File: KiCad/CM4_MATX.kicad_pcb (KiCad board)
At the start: 2 copper layers, 243.8 x 243.8 mm, 66 parts, among them IC1 USB2517-JZX, IC2 PI7C9X2G404SLBFDE, IC3 M24C04-RMN6TP, J1 72309-8014BLF, J10 72309-8014BLF, J11 10104110-0001LF, J12 SS-52100-002, J13 PCIe_x16, J14 PCIe_x16, J15 PCIe_x16, J16 GSD090012SEU, J17 Conn_02x04_Odd_Even, J18 ARJM11C7-502-AB-ER2-T, J19 Conn_02x20_Odd_Even, J20 Conn_02x04_Odd_Even, J3 Conn_01x22_Female, J5 Conn_01x22_Female, J6 1888811-1, J7 39-28-1243, J9 Conn_02x05_Odd_Even, M1 Fan_CPU_4pin, M2 Fan_CPU_4pin, U1 MAX6639ATE+, U10 MIC2019YM6-TR, U11 MIC2019YM6-TR, U12 MIC2019YM6-TR, U13 MIC2019YM6-TR, U14 MIC2019YM6-TR, U15 MIC2019YM6-TR, U16 MIC2019YM6-TR, U17 TCA9548ARGER, U18 PCF85263AT, U19 AP7363-10D, U3 FSUSB42MUX, U4 AP7363-10D, U5 AP2822CKETR-G1, U6 74LVC1G07GW, U7 TPD4EUSB30, U8 RT9742GGJ5, U9 TPD4EUSB30, Y2 Crystal

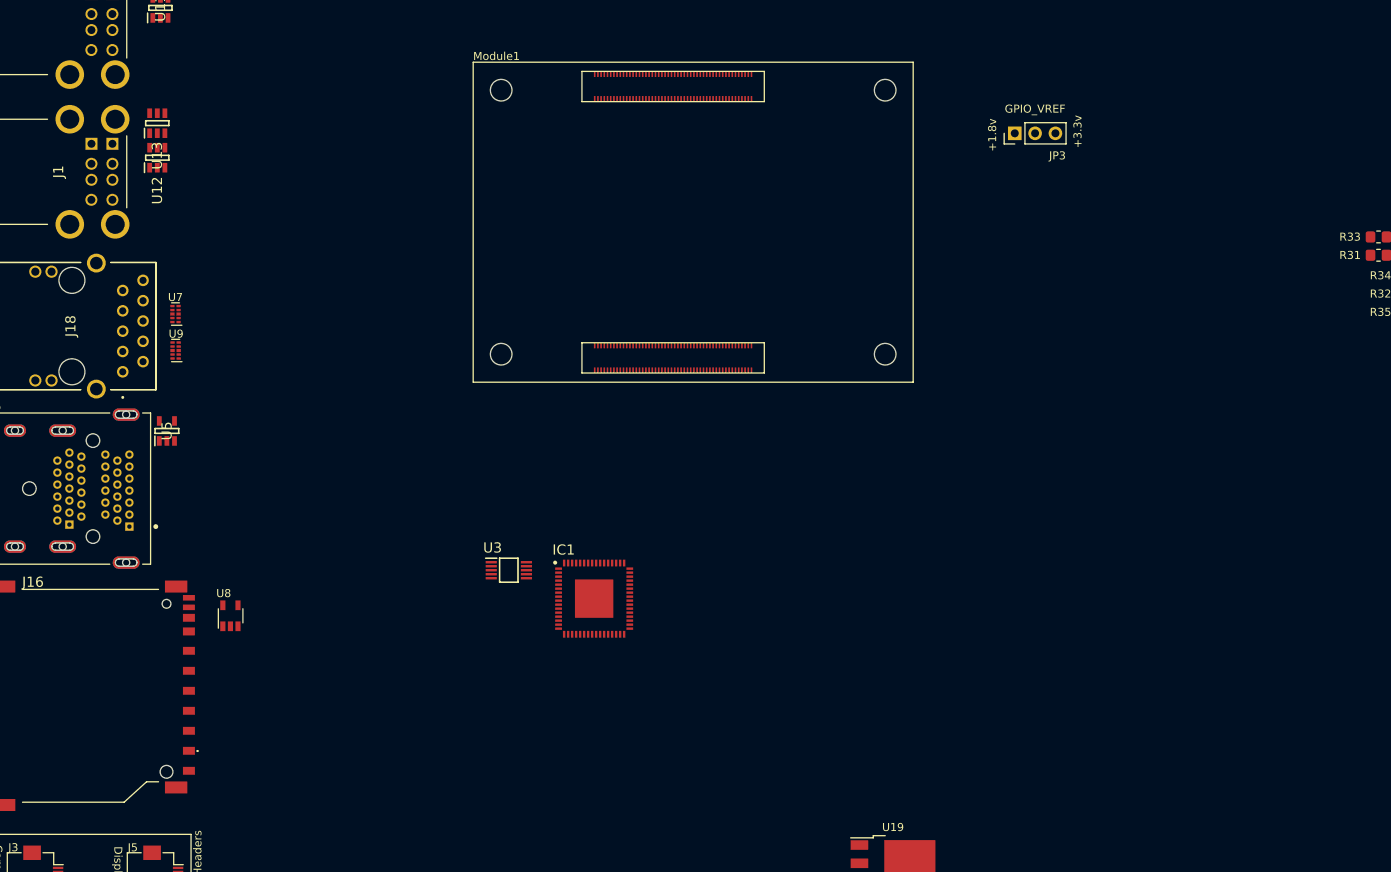
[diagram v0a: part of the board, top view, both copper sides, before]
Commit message: Updated CM4 footprints/symbols, mounting holes
This is in a bid to make it more manufactuerable by reducing the need for explanations and questions.
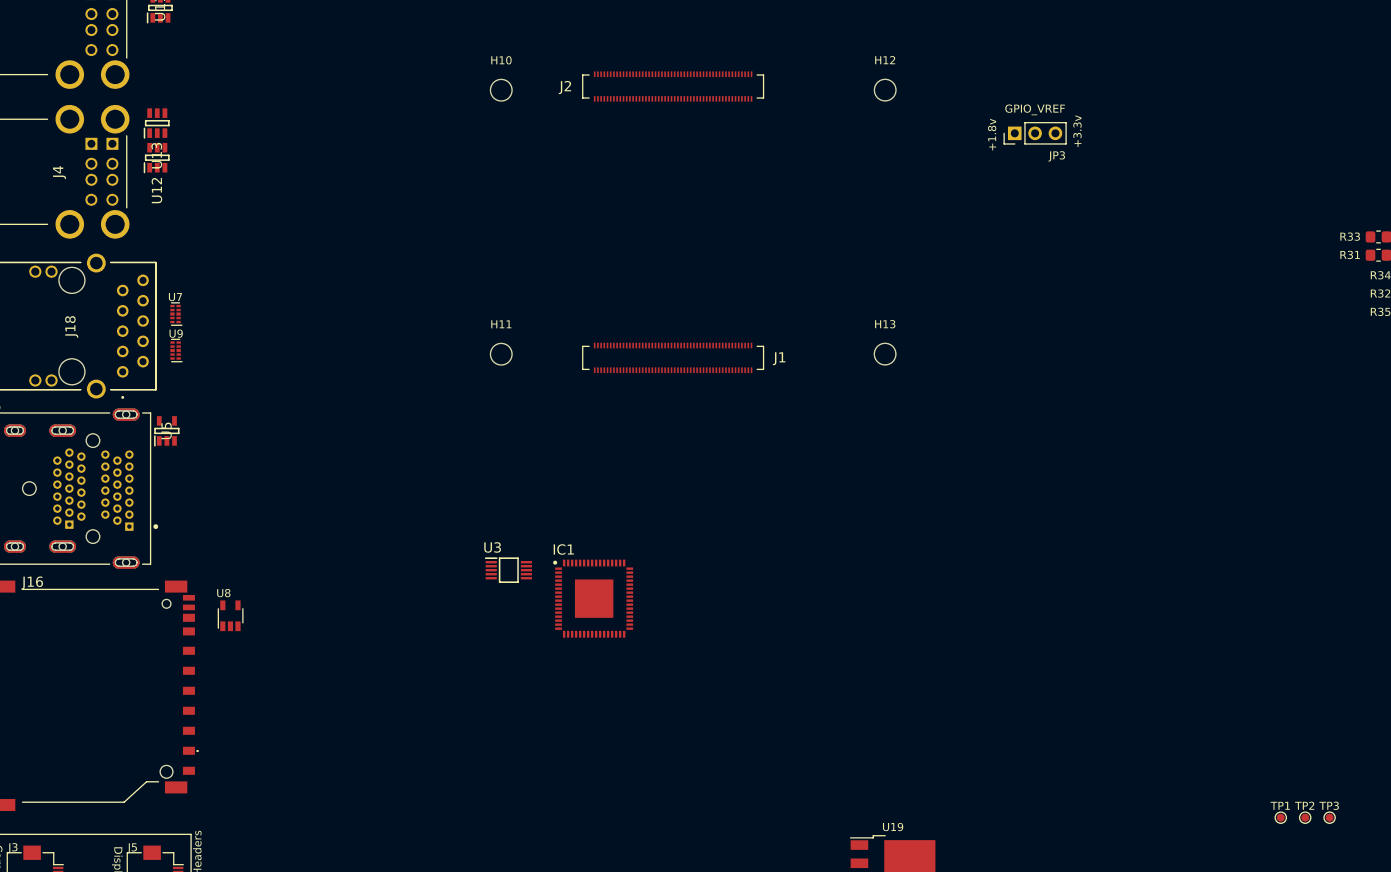
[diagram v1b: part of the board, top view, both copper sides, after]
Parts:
- removed Module1: ComputeModule4-CM4, CM4_MATX:rpiCM4
- added H10: MountingHole, MountingHole:MountingHole_2.7mm_M2.5, F.Cu at (102.7, 54.3)
- added H11: MountingHole, MountingHole:MountingHole_2.7mm_M2.5, F.Cu at (102.7, 87.3)
- added H12: MountingHole, MountingHole:MountingHole_2.7mm_M2.5, F.Cu at (150.7, 54.3)
- added H13: MountingHole, MountingHole:MountingHole_2.7mm_M2.5, F.Cu at (150.7, 87.3)
- added J1: CM4_B, CM4_MATX:DF40C100DS04V51_B, F.Cu at (124.2, 87.8)
- added J2: CM4_A, CM4_MATX:DF40C100DS04V51, F.Cu at (124.2, 53.8)
- added TP1: STATUS2, CM4_MATX:TestPoint_Pad_D1.0mm, F.Cu at (200.1, 145.2)
- added TP2: STATUS0, CM4_MATX:TestPoint_Pad_D1.0mm, F.Cu at (203.2, 145.2)
- added TP3: STATUS1, CM4_MATX:TestPoint_Pad_D1.0mm, F.Cu at (206.2, 145.2)
- C39: value C0.1u -> 0.1uF
- C69, C70: value C100n -> 100nF
- IC3: footprint CM4_MATX:SOIC127P600X175-8N -> _LibLoader:SOIC127P600X175-8N
- R30, R31, R32, R33, R34, R35, R5, R7: value R4.7k -> 4.7K
- Y2: value Crystal -> 32.768KHz
- renumbered J1 to J4
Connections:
- net Net-(IC2-Pad33) renamed /PCIe_Subsystem/PCIe_Switch/SLOTCLK
- IC2 pad 1: /PCIe_Subsystem/PCIe_Switch/+3.3v -> +3V3
- IC2 pad 113: /PCIe_Subsystem/PCIe_Switch/+3.3v -> +3V3
- IC2 pad 15: /PCIe_Subsystem/PCIe_Switch/+3.3vSB -> +3.3VA
- IC2 pad 49: /PCIe_Subsystem/PCIe_Switch/+3.3v -> +3V3
- IC2 pad 64: /PCIe_Subsystem/PCIe_Switch/+3.3v -> +3V3
- IC2 pad 79: /PCIe_Subsystem/PCIe_Switch/+3.3v -> +3V3
- IC2 pad 8: /PCIe_Subsystem/PCIe_Switch/+3.3v -> +3V3
- IC2 pad 82: /PCIe_Subsystem/PCIe_Switch/+3.3v -> +3V3
- IC2 pad 84: /PCIe_Subsystem/PCIe_Switch/+3.3v -> +3V3
- IC2 pad 96: /PCIe_Subsystem/PCIe_Switch/+3.3v -> +3V3
- IC3 pad 8: /PCIe_Subsystem/PCIe_Switch/+3.3v -> +3V3
- U19 pad 1: /PCIe_Subsystem/PCIe_Switch/+3.3vSB -> +3.3VA
- U4 pad 1: /PCIe_Subsystem/PCIe_Switch/+3.3v -> +3V3
